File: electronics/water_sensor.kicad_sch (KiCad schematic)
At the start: 0 parts

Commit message: from Legion
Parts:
- added J11: ~, HeavyDuty:water_sensor_rods, symbol HeavyDuty:water_sensor_rods
- added J7: Conn_01x02, Connector_Samtec_HPM_THT:Samtec_HPM-02-01-x-S_Straight_1x02_Pitch5.08mm, symbol Connector_Generic:Conn_01x02
- added J9: water_sensor_conn, TerminalBlock:TerminalBlock_Xinya_XY308-2.54-6P_1x06_P2.54mm_Horizontal, symbol Connector_Generic:Conn_01x06
- added U12: ~, HeavyDuty:2_water_sensor_rods, symbol HeavyDuty:water_sesnor_binary
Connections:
- new net: J11.2 (lvl_1), J9.2 (Pin_2)
- new net: J11.3 (lvl_2), J9.3 (Pin_3)
- new net: J11.4 (lvl_3), J9.4 (Pin_4)
- new net: J11.5 (lvl_4), J9.5 (Pin_5)
- new net: J11.6 (lvl_5), J9.6 (Pin_6)
- new net COM: J11.1 (COM), J7.1 (Pin_1), J9.1 (Pin_1)
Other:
- note added: "round PCB shape with 6 rods in the middle"

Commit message: flight back. different layout. start analog ui
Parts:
- removed J9: water_sensor_conn, TerminalBlock:TerminalBlock_Xinya_XY308-2.54-6P_1x06_P2.54mm_Horizontal, symbol Connector_Generic:Conn_01x06
- added J9: water_sensor_conn, TerminalBlock:TerminalBlock_Xinya_XY308-2.54-5P_1x05_P2.54mm_Horizontal, symbol Connector_Generic:Conn_01x05
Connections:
- net COM: now also J9.1 (Pin_1)
- net at J11.2 (lvl_1): now also J9.2 (Pin_2)
- net at J11.3 (lvl_2): now also J9.3 (Pin_3)
- net at J11.4 (lvl_3): now also J9.4 (Pin_4)
- net at J11.5 (lvl_4): now also J9.5 (Pin_5)
- no-connect marks 0 -> 1
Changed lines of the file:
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@@
 		(color 0 0 0 0)
 	)
+	(no_connect
+		(at 119.38 76.2)
+	)
 	(wire
 		(pts
@@
 		(pts
 			(xy 115.57 88.9) (xy 119.38 88.9)
-		)
-		(stroke
-			(width 0)
-			(type default)
-		)
-	)
-	(wire
-		(pts
-			(xy 111.76 76.2) (xy 119.38 76.2)
 		)
 		(stroke
@@
 	)
 	(symbol
-		(lib_id "Connector_Generic:Conn_01x06")
+		(lib_id "Connector_Generic:Conn_01x05")
 		(at 106.68 83.82 180)
 		(unit 1)
@@
 		(on_board yes)
 		(dnp no)
+		(fields_autoplaced yes)
 		(property "Reference" "J9"
-			(at 104.14 83.8201 0)
-			(effects
-				(font
-					(size 1.27 1.27)
-				)
-				(justify left)
+			(at 106.68 72.39 0)
+			(effects
+				(font
+					(size 1.27 1.27)
+				)
 			)
 		)
 		(property "Value" "water_sensor_conn"
-			(at 104.14 81.2801 0)
-			(effects
-				(font
-					(size 1.27 1.27)
-				)
-				(justify left)
-			)
-		)
-		(property "Footprint" "TerminalBlock:TerminalBlock_Xinya_XY308-2.54-6P_1x06_P2.54mm_Horizontal"
+			(at 106.68 74.93 0)
+			(effects
+				(font
+					(size 1.27 1.27)
+				)
+			)
+		)
+		(property "Footprint" "TerminalBlock:TerminalBlock_Xinya_XY308-2.54-5P_1x05_P2.54mm_Horizontal"
 			(at 106.68 83.82 0)
 			(effects
@@
 			)
 		)
-		(property "Description" "Generic connector, single row, 01x06, script generated (kicad-library-utils/schlib/autogen/connector/)"
+		(property "Description" "Generic connector, single row, 01x05, script generated (kicad-library-utils/schlib/autogen/connector/)"
 			(at 106.68 83.82 0)
 			(effects
@@
 			)
 		)
+		(pin "4"
+		)
 		(pin "2"
 		)
-		(pin "4"
-		)
 		(pin "5"
 		)
-		(pin "6"
-		)
 		(pin "1"

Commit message: no tracks, but placement looks good
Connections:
- net at U12.1 (COM): now also J7.1 (Pin_1)
- net at U12.2 (LVL_0): now also J7.2 (Pin_2)
- net COM: no longer names the net of J11.1 (COM), J9.1 (Pin_1)
- net COM: no longer J7.1 (Pin_1)
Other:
- moved on the sheet: U12
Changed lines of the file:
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@@
 	(generator_version "8.0")
 	(paper "A4")
-	(junction
-		(at 115.57 114.3)
-		(diameter 0)
-		(color 0 0 0 0)
-	)
-	(junction
-		(at 115.57 88.9)
-		(diameter 0)
-		(color 0 0 0 0)
-	)
 	(no_connect
 		(at 119.38 76.2)
-	)
-	(wire
-		(pts
-			(xy 115.57 92.71) (xy 115.57 88.9)
-		)
-		(stroke
-			(width 0)
-			(type default)
-		)
 	)
 	(wire
@@
 	(wire
 		(pts
-			(xy 113.03 114.3) (xy 115.57 114.3)
-		)
-		(stroke
-			(width 0)
-			(type default)
-		)
-	)
-	(wire
-		(pts
-			(xy 115.57 114.3) (xy 119.38 114.3)
-		)
-		(stroke
-			(width 0)
-			(type default)
-		)
-	)
-	(wire
-		(pts
-			(xy 115.57 119.38) (xy 115.57 114.3)
+			(xy 113.03 114.3) (xy 121.92 114.3)
 		)
 		(stroke
@@
 	(wire
 		(pts
-			(xy 113.03 111.76) (xy 119.38 111.76)
+			(xy 113.03 111.76) (xy 121.92 111.76)
 		)
 		(stroke
@@
 	(wire
 		(pts
-			(xy 121.92 92.71) (xy 115.57 92.71)
-		)
-		(stroke
-			(width 0)
-			(type default)
-		)
-	)
-	(wire
-		(pts
-			(xy 111.76 88.9) (xy 115.57 88.9)
-		)
-		(stroke
-			(width 0)
-			(type default)
-		)
-	)
-	(wire
-		(pts
-			(xy 115.57 88.9) (xy 119.38 88.9)
+			(xy 111.76 88.9) (xy 119.38 88.9)
 		)
 		(stroke
@@
 		)
 	)
-	(wire
-		(pts
-			(xy 120.65 119.38) (xy 115.57 119.38)
-		)
-		(stroke
-			(width 0)
-			(type default)
-		)
-	)
 	(text "round PCB shape with 6 rods in the middle"
 		(exclude_from_sim no)
@@
 		)
 	)
-	(hierarchical_label "COM"
-		(shape passive)
-		(at 120.65 119.38 0)
-		(fields_autoplaced yes)
-		(effects
-			(font
-				(size 1.27 1.27)
-			)
-			(justify left)
-		)
-	)
-	(hierarchical_label "COM"
-		(shape passive)
-		(at 121.92 92.71 0)
-		(fields_autoplaced yes)
-		(effects
-			(font
-				(size 1.27 1.27)
-			)
-			(justify left)
-		)
-	)
 	(symbol
 		(lib_id "HeavyDuty:water_sesnor_binary")
-		(at 124.46 113.03 0)
+		(at 128.27 113.03 0)
 		(unit 1)
 		(exclude_from_sim no)
@@
 		(fields_autoplaced yes)
 		(property "Reference" "U12"
-			(at 129.54 112.3949 0)
+			(at 133.35 112.3949 0)
 			(effects
 				(font
@@
 		)
 		(property "Value" "~"
-			(at 129.54 114.3 0)
+			(at 133.35 114.3 0)
 			(effects
 				(font
@@
 		)
 		(property "Footprint" "HeavyDuty:2_water_sensor_rods"
-			(at 124.46 113.03 0)
+			(at 128.27 113.03 0)
 			(effects
 				(font
@@
 		)
 		(property "Datasheet" ""
-			(at 124.46 113.03 0)
+			(at 128.27 113.03 0)
 			(effects
 				(font
@@
 		)
 		(property "Description" ""
-			(at 124.46 113.03 0)
+			(at 128.27 113.03 0)
 			(effects
 				(font

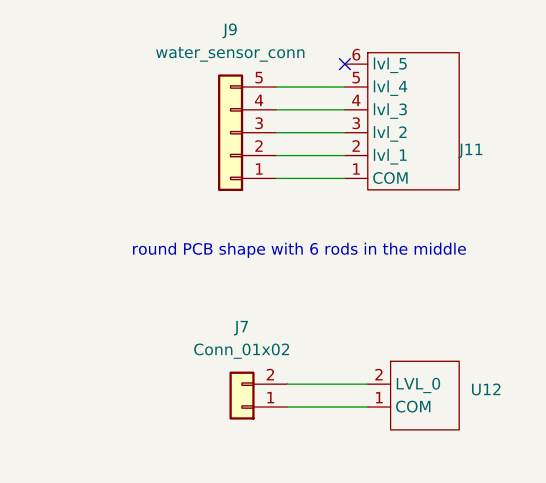
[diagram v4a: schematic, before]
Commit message: start to create BOM and finalising symbol fields
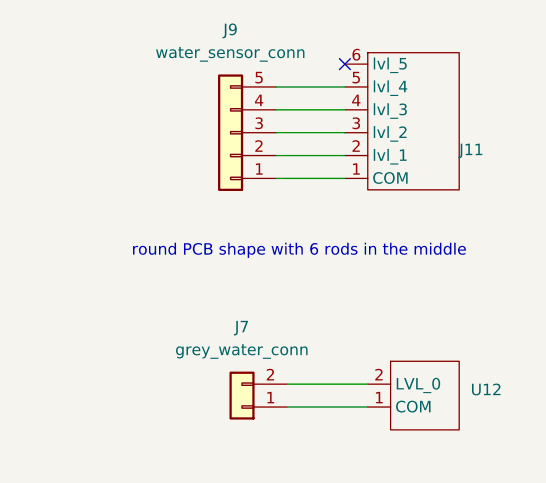
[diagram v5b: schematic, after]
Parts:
- J7: value Conn_01x02 -> grey_water_conn
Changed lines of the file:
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@@
 			)
 		)
-		(property "Value" "Conn_01x02"
+		(property "Value" "grey_water_conn"
 			(at 107.95 107.95 0)
 			(effects
